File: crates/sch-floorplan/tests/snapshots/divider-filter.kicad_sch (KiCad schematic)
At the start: 3 parts

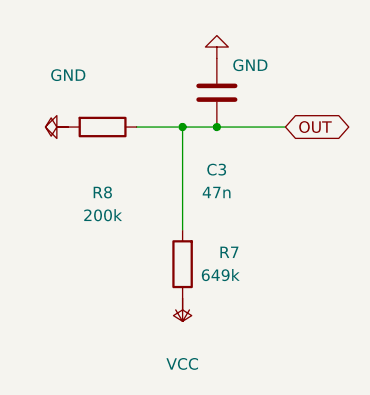
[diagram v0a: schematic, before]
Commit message: sch-doc: pick the smallest standard page from an A5-first ladder
A four-part circuit on A4 is a drawing stranded in one corner of an
empty sheet; the critic scored that a point worse than the snug custom
page it replaced. Starting the ladder at A5 keeps the frame close to
the content while every sheet still lands on a size KiCad and a printer
recognise.

Re-blessed the five snapshots whose critic score held at or above their
pre-change score. grid-demo is left at its baseline: it renders 7 where
it used to render 9.

Claude-Session: https://claude.ai/code/session_01GyGRY43X8yBh8WS1tjEmFz
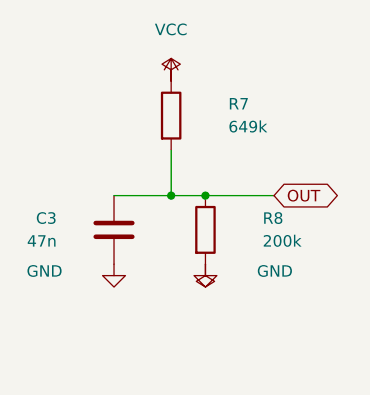
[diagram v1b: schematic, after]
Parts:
- C3, R7, R8: ap_block (none) -> divider
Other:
- moved on the sheet: C3, R7, R8
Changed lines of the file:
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@@
 	(generator "gordian")
 	(generator_version "0.1")
-	(paper "User" 57.91 97.47)
+	(paper "A5")
 	(title_block
 		(title "divider-filter")
+		(rev "1.0")
 	)
 	(global_label "OUT"
 		(shape bidirectional)
-		(at 41.910000000000004 25.4 0)
+		(at 40.64 33.02 0)
 		(effects (font (size 1.27 1.27)) (justify left))
 	)
 	(wire
 		(pts
-			(xy 25.4 25.4) (xy 30.48 25.4)
-		)
-		(stroke (width 0) (type default))
-	)
-	(wire
-		(pts
-			(xy 30.48 25.4) (xy 34.29 25.4)
-		)
-		(stroke (width 0) (type default))
-	)
-	(wire
-		(pts
-			(xy 30.48 36.83) (xy 30.48 25.4)
-		)
-		(stroke (width 0) (type default))
-	)
-	(wire
-		(pts
-			(xy 34.29 25.4) (xy 41.910000000000004 25.4)
+			(xy 22.86 33.02) (xy 29.21 33.02)
+		)
+		(stroke (width 0) (type default))
+	)
+	(wire
+		(pts
+			(xy 29.21 27.94) (xy 29.21 33.02)
+		)
+		(stroke (width 0) (type default))
+	)
+	(wire
+		(pts
+			(xy 29.21 33.02) (xy 33.02 33.02)
+		)
+		(stroke (width 0) (type default))
+	)
+	(wire
+		(pts
+			(xy 33.02 33.02) (xy 40.64 33.02)
 		)
 		(stroke (width 0) (type default))
 	)
 	(junction
-		(at 30.48 25.4)
+		(at 29.21 33.02)
 		(diameter 0)
 		(color 0 0 0 0)
 	)
 	(junction
-		(at 34.29 25.4)
+		(at 33.02 33.02)
 		(diameter 0)
 		(color 0 0 0 0)
@@
 	(symbol
 		(lib_id "power:PWR_FLAG")
-		(at 17.78 25.4 90)
+		(at 33.02 40.64 180)
 		(unit 1)
 		(exclude_from_sim no)
@@
 		(dnp no)
 		(property "Reference" "#FLG_GND"
-			(at 24.13 24.13 270)
+			(at 39.370000000000005 39.37 0)
 			(effects (font (size 1.27 1.27)) (justify left) (hide yes))
 		)
 		(property "Value" "PWR_FLAG"
-			(at 24.13 26.669999999999998 270)
-			(effects (font (size 1.27 1.27)) (justify left) (hide yes))
-		)
-		(property "Footprint" ""
-			(at 17.78 25.4 0)
+			(at 39.370000000000005 41.910000000000004 0)
+			(effects (font (size 1.27 1.27)) (justify left) (hide yes))
+		)
+		(property "Footprint" ""
+			(at 33.02 40.64 0)
 			(effects (font (size 1.27 1.27)) (hide yes))
 		)
@@
 	(symbol
 		(lib_id "power:PWR_FLAG")
-		(at 30.48 44.45 180)
+		(at 29.21 20.32 0)
 		(unit 1)
 		(exclude_from_sim no)
@@
 		(dnp no)
 		(property "Reference" "#FLG_VCC"
-			(at 36.830000000000005 43.18 0)
+			(at 35.56 19.05 0)
 			(effects (font (size 1.27 1.27)) (justify left) (hide yes))
 		)
 		(property "Value" "PWR_FLAG"
-			(at 36.830000000000005 45.720000000000006 0)
-			(effects (font (size 1.27 1.27)) (justify left) (hide yes))
-		)
-		(property "Footprint" ""
-			(at 30.48 44.45 0)
+			(at 35.56 21.59 0)
+			(effects (font (size 1.27 1.27)) (justify left) (hide yes))
+		)
+		(property "Footprint" ""
+			(at 29.21 20.32 0)
 			(effects (font (size 1.27 1.27)) (hide yes))
 		)
@@
 	(symbol
 		(lib_id "power:GND")
-		(at 17.78 25.4 270)
+		(at 33.02 40.64 0)
 		(unit 1)
 		(exclude_from_sim no)
@@
 		(dnp no)
 		(property "Reference" "#PWR_GND_0"
-			(at 24.13 24.13 90)
+			(at 39.370000000000005 39.37 0)
 			(effects (font (size 1.27 1.27)) (justify left) (hide yes))
 		)
 		(property "Value" "GND"
-			(at 17.78 19.68 90)
+			(at 38.74 41.44 0)
+			(effects (font (size 1.27 1.27)) (justify left))
+		)
+		(property "Footprint" ""
+			(at 33.02 40.64 0)
+			(effects (font (size 1.27 1.27)) (hide yes))
+		)
+		(instances
+			(project ""
+				(path "/78c1c215-99f1-55bb-ac37-0886ad3d1a9e"
+					(reference "#PWR_GND_0")
+					(unit 1)
+				)
+			)
+		)
+	)
+	(symbol
+		(lib_id "power:GND")
+		(at 22.86 40.64 0)
+		(unit 1)
+		(exclude_from_sim no)
+		(in_bom yes)
+		(on_board yes)
+		(dnp no)
+		(property "Reference" "#PWR_GND_1"
+			(at 29.209999999999997 39.37 0)
+			(effects (font (size 1.27 1.27)) (justify left) (hide yes))
+		)
+		(property "Value" "GND"
+			(at 17.14 41.44 0)
+			(effects (font (size 1.27 1.27)) (justify right))
+		)
+		(property "Footprint" ""
+			(at 22.86 40.64 0)
+			(effects (font (size 1.27 1.27)) (hide yes))
+		)
+		(instances
+			(project ""
+				(path "/78c1c215-99f1-55bb-ac37-0886ad3d1a9e"
+					(reference "#PWR_GND_1")
+					(unit 1)
+				)
+			)
+		)
+	)
+	(symbol
+		(lib_id "power:VCC")
+		(at 29.21 20.32 0)
+		(unit 1)
+		(exclude_from_sim no)
+		(in_bom yes)
+		(on_board yes)
+		(dnp no)
+		(property "Reference" "#PWR_VCC_0"
+			(at 35.56 19.05 0)
+			(effects (font (size 1.27 1.27)) (justify left) (hide yes))
+		)
+		(property "Value" "VCC"
+			(at 29.21 14.6 0)
 			(effects (font (size 1.27 1.27)))
 		)
 		(property "Footprint" ""
-			(at 17.78 25.4 0)
-			(effects (font (size 1.27 1.27)) (hide yes))
-		)
-		(instances
-			(project ""
-				(path "/78c1c215-99f1-55bb-ac37-0886ad3d1a9e"
-					(reference "#PWR_GND_0")
-					(unit 1)
-				)
-			)
-		)
-	)
-	(symbol
-		(lib_id "power:GND")
-		(at 34.29 17.78 180)
-		(unit 1)
-		(exclude_from_sim no)
-		(in_bom yes)
-		(on_board yes)
-		(dnp no)
-		(property "Reference" "#PWR_GND_1"
-			(at 40.64 16.51 0)
-			(effects (font (size 1.27 1.27)) (justify left) (hide yes))
-		)
-		(property "Value" "GND"
-			(at 40.01 18.58 0)
-			(effects (font (size 1.27 1.27)) (justify left))
-		)
-		(property "Footprint" ""
-			(at 34.29 17.78 0)
-			(effects (font (size 1.27 1.27)) (hide yes))
-		)
-		(instances
-			(project ""
-				(path "/78c1c215-99f1-55bb-ac37-0886ad3d1a9e"
-					(reference "#PWR_GND_1")
-					(unit 1)
-				)
-			)
-		)
-	)
-	(symbol
-		(lib_id "power:VCC")
-		(at 30.48 44.45 180)
-		(unit 1)
-		(exclude_from_sim no)
-		(in_bom yes)
-		(on_board yes)
-		(dnp no)
-		(property "Reference" "#PWR_VCC_0"
-			(at 36.830000000000005 43.18 0)
-			(effects (font (size 1.27 1.27)) (justify left) (hide yes))
-		)
-		(property "Value" "VCC"
-			(at 30.48 51.77 0)
-			(effects (font (size 1.27 1.27)))
-		)
-		(property "Footprint" ""
-			(at 30.48 44.45 0)
+			(at 29.21 20.32 0)
 			(effects (font (size 1.27 1.27)) (hide yes))
 		)
@@
 	(symbol
 		(lib_id "Device:C")
-		(at 34.29 21.59 180)
+		(at 22.86 36.83 0)
 		(unit 1)
 		(exclude_from_sim no)
@@
 		(dnp no)
 		(property "Reference" "C3"
-			(at 34.29 30.18 0)
-			(effects (font (size 1.27 1.27)))
+			(at 16.51 35.56 0)
+			(effects (font (size 1.27 1.27)) (justify right))
 		)
 		(property "Value" "47n"
-			(at 34.29 32.72 0)
-			(effects (font (size 1.27 1.27)))
-		)
-		(property "Footprint" ""
-			(at 34.29 21.59 0)
+			(at 16.51 38.1 0)
+			(effects (font (size 1.27 1.27)) (justify right))
+		)
+		(property "Footprint" ""
+			(at 22.86 36.83 0)
+			(effects (font (size 1.27 1.27)) (hide yes))
+		)
+		(property "ap_block" "divider"
+			(at 22.86 36.83 0)
 			(effects (font (size 1.27 1.27)) (hide yes))
 		)
@@
 	(symbol
 		(lib_id "Device:R")
-		(at 30.48 40.64 180)
+		(at 29.21 24.13 0)
 		(unit 1)
 		(exclude_from_sim no)
@@
 		(dnp no)
 		(property "Reference" "R7"
-			(at 36.83 39.37 0)
+			(at 35.56 22.86 0)
 			(effects (font (size 1.27 1.27)) (justify left))
 		)
 		(property "Value" "649k"
-			(at 36.83 41.91 0)
-			(effects (font (size 1.27 1.27)) (justify left))
-		)
-		(property "Footprint" ""
-			(at 30.48 40.64 0)
+			(at 35.56 25.4 0)
+			(effects (font (size 1.27 1.27)) (justify left))
+		)
+		(property "Footprint" ""
+			(at 29.21 24.13 0)
+			(effects (font (size 1.27 1.27)) (hide yes))
+		)
+		(property "ap_block" "divider"
+			(at 29.21 24.13 0)
 			(effects (font (size 1.27 1.27)) (hide yes))
 		)
@@
 	(symbol
 		(lib_id "Device:R")
-		(at 21.59 25.4 270)
+		(at 33.02 36.83 0)
 		(unit 1)
 		(exclude_from_sim no)
@@
 		(dnp no)
 		(property "Reference" "R8"
-			(at 21.59 32.72 90)
-			(effects (font (size 1.27 1.27)))
+			(at 39.37 35.56 0)
+			(effects (font (size 1.27 1.27)) (justify left))
 		)
 		(property "Value" "200k"
-			(at 21.59 35.26 90)
-			(effects (font (size 1.27 1.27)))
-		)
-		(property "Footprint" ""
-			(at 21.59 25.4 0)
-			(effects (font (size 1.27 1.27)) (hide yes))
-		)
+			(at 39.37 38.1 0)
+			(effects (font (size 1.27 1.27)) (justify left))
+		)
+		(property "Footprint" ""
+			(at 33.02 36.83 0)
+			(effects (font (size 1.27 1.27)) (hide yes))
+		)
+		(property "ap_block" "divider"
+			(at 33.02 36.83 0)
+			(effects (font (size 1.27 1.27)) (hide yes))
+		)
